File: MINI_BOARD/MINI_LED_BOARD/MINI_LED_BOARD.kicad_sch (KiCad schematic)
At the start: 38 parts, among them J1 Conn_ARM_SWD_TagConnect_TC2030, J2 430450428, U1 MSPM0C1103SDDFR, U2 TCAN334, U3 NCV891330PD50R2G, U4 TPS76333DBVR

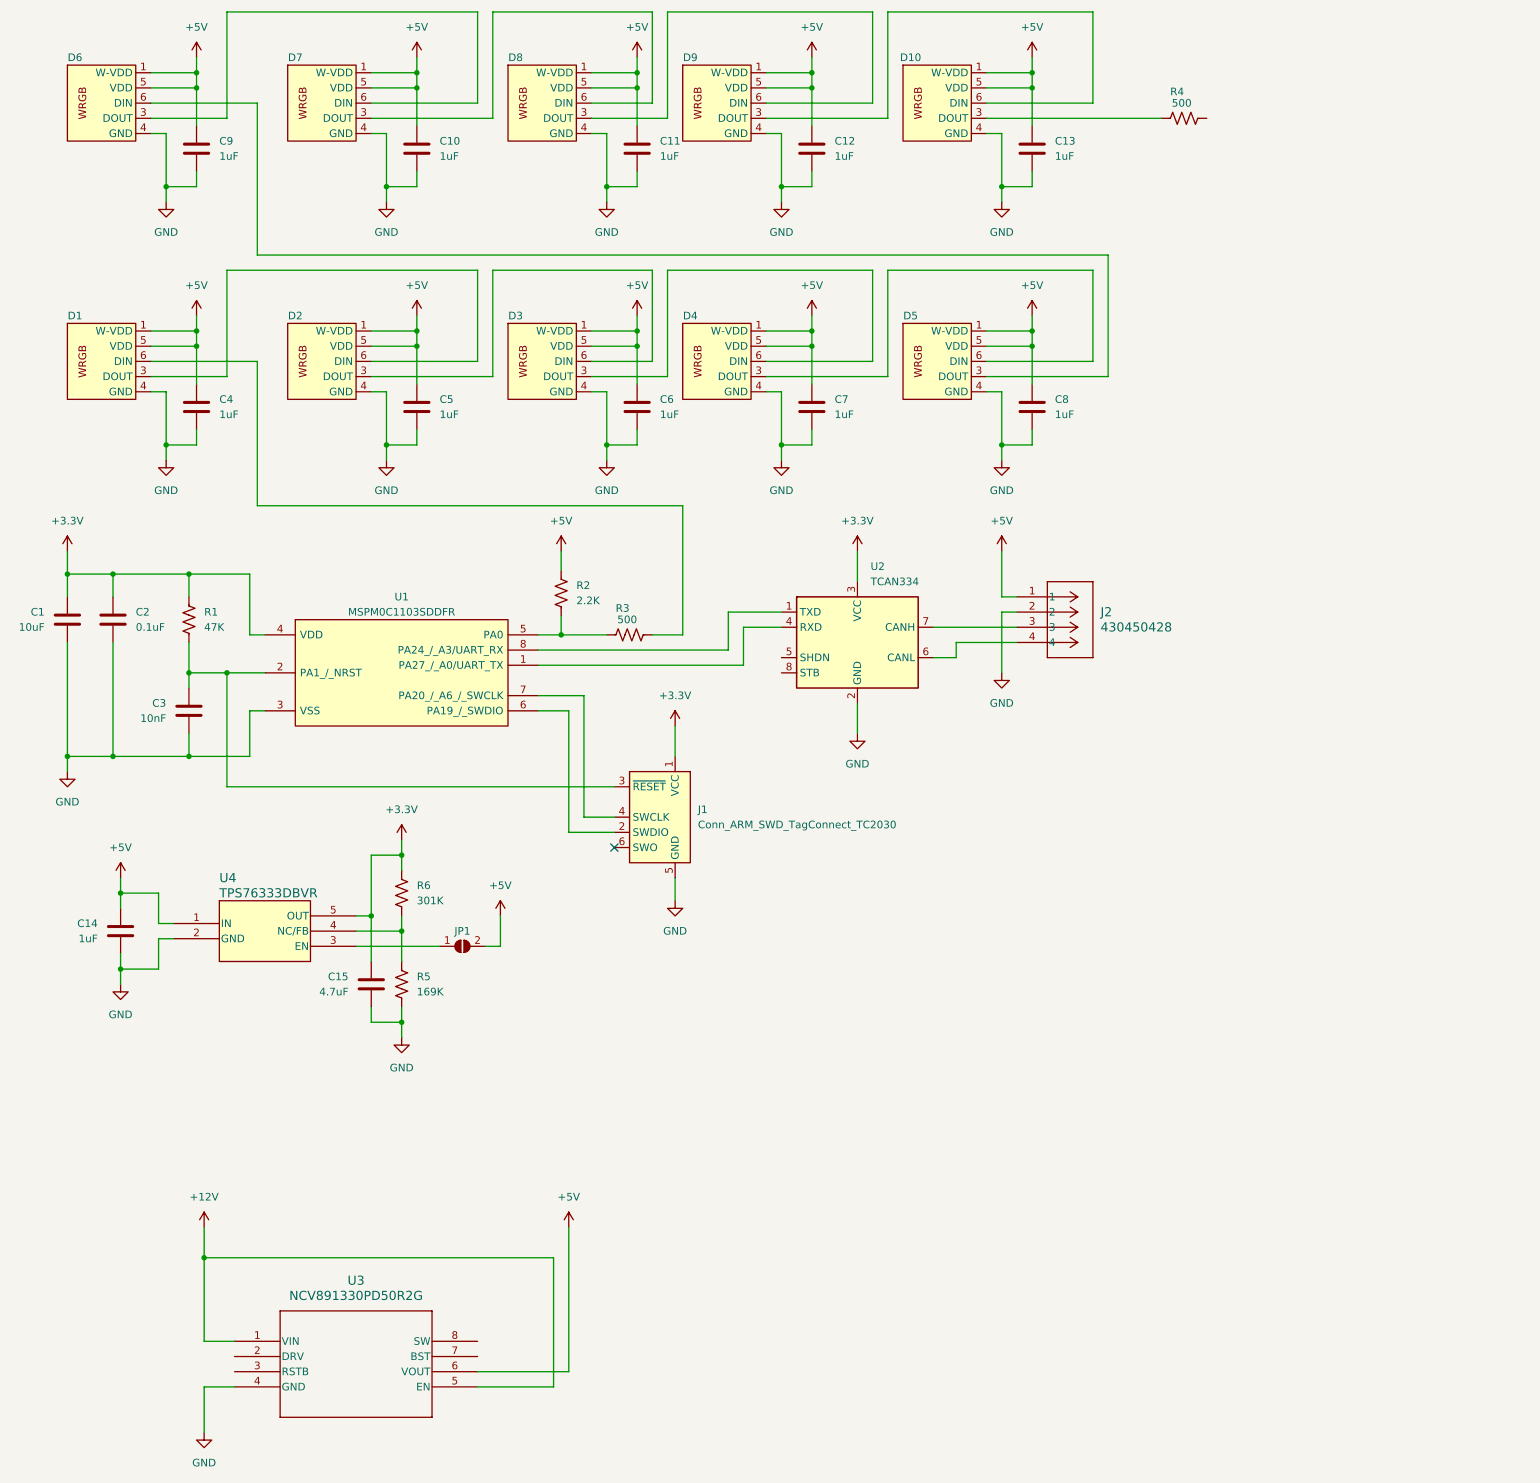
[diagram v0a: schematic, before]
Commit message: Add more footprints and adjust layout placements
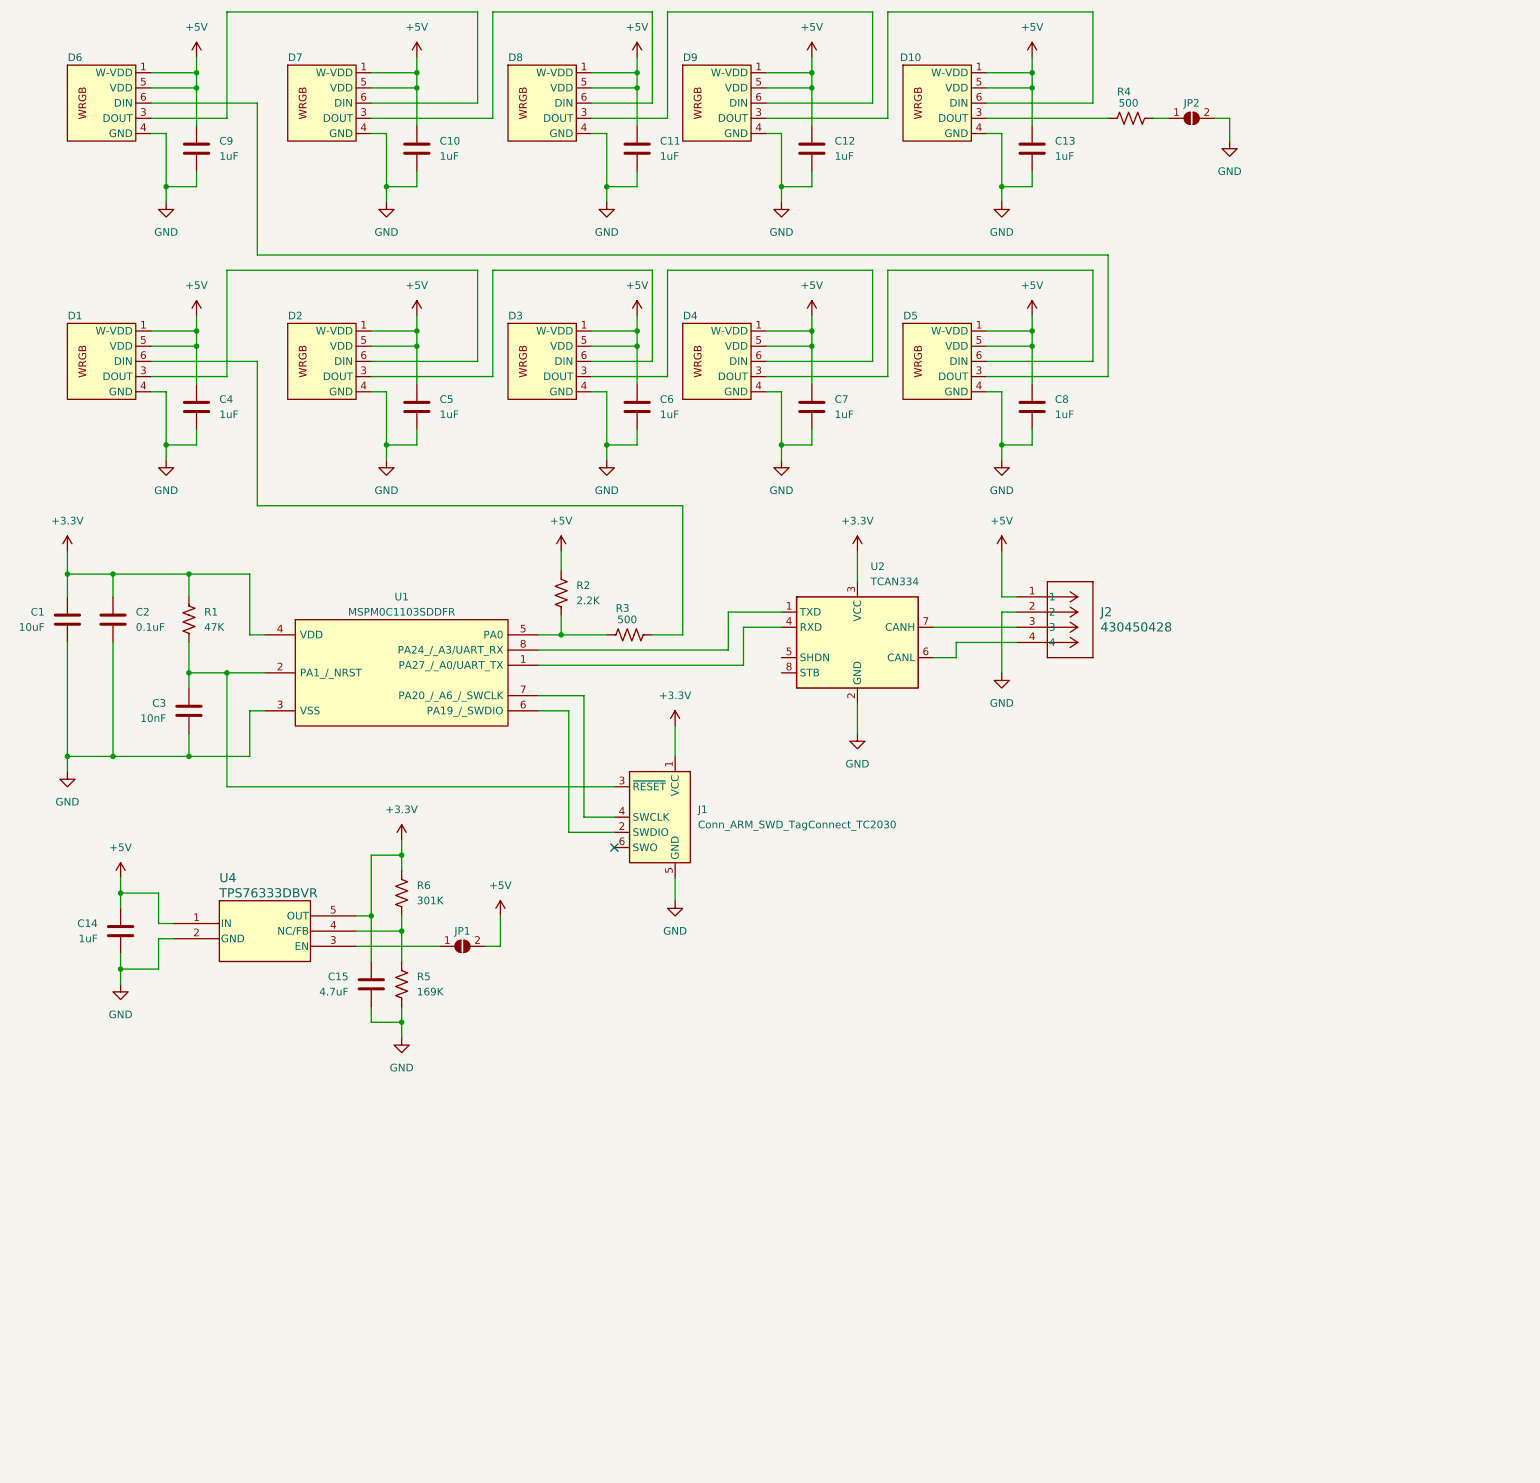
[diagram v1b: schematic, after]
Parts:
- removed U3: NCV891330PD50R2G, SOIC8_3P9X4P9_ONS, symbol NCV891330PD50R2G:NCV891330PD50R2G
- added JP2: SolderJumper_2_Open, Jumper:SolderJumper-2_P1.3mm_Open_RoundedPad1.0x1.5mm, symbol Jumper:SolderJumper_2_Open
- JP1: footprint (none) -> Jumper:SolderJumper-2_P1.3mm_Open_RoundedPad1.0x1.5mm
- U2: footprint (none) -> Package_TO_SOT_SMD:SOT-23-8_Handsoldering
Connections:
- net GND: now also JP2.2 (B)
- net at R4.2: now also JP2.1 (A)
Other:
- moved on the sheet: R4
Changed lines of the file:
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@@
   (junction (at 180.34 46.99) (diameter 0) (color 0 0 0 0)
   )
-  (junction (at 46.99 226.06) (diameter 0) (color 0 0 0 0)
-  )
   (junction (at 80.01 171.45) (diameter 0) (color 0 0 0 0)
   )
@@
     (stroke (width 0) (type default))
   )
-  (wire (pts (xy 107.95 245.11) (xy 107.95 220.98))
-    (stroke (width 0) (type default))
-  )
   (wire (pts (xy 143.51 49.53) (xy 143.51 46.99))
     (stroke (width 0) (type default))
@@
     (stroke (width 0) (type default))
   )
+  (wire (pts (xy 218.44 39.37) (xy 218.44 35.56))
+    (stroke (width 0) (type default))
+  )
   (wire (pts (xy 111.76 76.2) (xy 121.92 76.2))
     (stroke (width 0) (type default))
@@
     (stroke (width 0) (type default))
   )
-  (wire (pts (xy 52.07 247.65) (xy 46.99 247.65))
-    (stroke (width 0) (type default))
-  )
   (wire (pts (xy 95.25 35.56) (xy 95.25 17.78))
     (stroke (width 0) (type default))
@@
     (stroke (width 0) (type default))
   )
-  (wire (pts (xy 105.41 226.06) (xy 46.99 226.06))
-    (stroke (width 0) (type default))
-  )
   (wire (pts (xy 134.62 118.11) (xy 143.51 118.11))
     (stroke (width 0) (type default))
@@
     (stroke (width 0) (type default))
   )
-  (wire (pts (xy 105.41 247.65) (xy 105.41 226.06))
-    (stroke (width 0) (type default))
-  )
   (wire (pts (xy 185.42 71.12) (xy 185.42 68.58))
     (stroke (width 0) (type default))
@@
     (stroke (width 0) (type default))
   )
-  (wire (pts (xy 46.99 247.65) (xy 46.99 255.27))
-    (stroke (width 0) (type default))
-  )
   (wire (pts (xy 198.12 78.74) (xy 198.12 58.42))
     (stroke (width 0) (type default))
@@
     (stroke (width 0) (type default))
   )
-  (wire (pts (xy 52.07 240.03) (xy 46.99 240.03))
-    (stroke (width 0) (type default))
-  )
   (wire (pts (xy 44.45 111.76) (xy 44.45 115.57))
     (stroke (width 0) (type default))
@@
     (stroke (width 0) (type default))
   )
+  (wire (pts (xy 208.28 35.56) (xy 205.74 35.56))
+    (stroke (width 0) (type default))
+  )
   (wire (pts (xy 140.97 78.74) (xy 161.29 78.74))
     (stroke (width 0) (type default))
@@
     (stroke (width 0) (type default))
   )
-  (wire (pts (xy 177.8 35.56) (xy 207.01 35.56))
+  (wire (pts (xy 177.8 35.56) (xy 198.12 35.56))
     (stroke (width 0) (type default))
   )
@@
     (stroke (width 0) (type default))
   )
-  (wire (pts (xy 92.71 247.65) (xy 105.41 247.65))
-    (stroke (width 0) (type default))
-  )
   (wire (pts (xy 74.93 27.94) (xy 82.55 27.94))
     (stroke (width 0) (type default))
@@
     (stroke (width 0) (type default))
   )
-  (wire (pts (xy 46.99 226.06) (xy 46.99 220.98))
-    (stroke (width 0) (type default))
-  )
   (wire (pts (xy 185.42 27.94) (xy 185.42 25.4))
     (stroke (width 0) (type default))
@@
     (stroke (width 0) (type default))
   )
-  (wire (pts (xy 46.99 226.06) (xy 46.99 240.03))
-    (stroke (width 0) (type default))
-  )
   (wire (pts (xy 50.8 35.56) (xy 38.1 35.56))
     (stroke (width 0) (type default))
@@
     (stroke (width 0) (type default))
   )
+  (wire (pts (xy 218.44 35.56) (xy 215.9 35.56))
+    (stroke (width 0) (type default))
+  )
   (wire (pts (xy 95.25 78.74) (xy 95.25 60.96))
     (stroke (width 0) (type default))
@@
     (stroke (width 0) (type default))
   )
-  (wire (pts (xy 92.71 245.11) (xy 107.95 245.11))
-    (stroke (width 0) (type default))
-  )
   (wire (pts (xy 127 121.92) (xy 121.92 121.92))
     (stroke (width 0) (type default))
@@
     )
   )
-  (symbol (lib_id "Device:R_US") (at 210.82 35.56 90) (unit 1)
+  (symbol (lib_id "Device:R_US") (at 201.93 35.56 90) (unit 1)
     (in_bom yes) (on_board yes) (dnp no)
-    (property "Reference" "R4" (at 210.82 31.115 90)
+    (property "Reference" "R4" (at 201.93 31.115 90)
       (effects (font (size 1.27 1.27)) (justify left))
     )
-    (property "Value" "500" (at 212.09 33.02 90)
+    (property "Value" "500" (at 203.2 33.02 90)
       (effects (font (size 1.27 1.27)) (justify left))
     )
-    (property "Footprint" "Resistor_SMD:R_0603_1608Metric_Pad0.98x0.95mm_HandSolder" (at 211.074 34.544 90)
+    (property "Footprint" "Resistor_SMD:R_0603_1608Metric_Pad0.98x0.95mm_HandSolder" (at 202.184 34.544 90)
       (effects (font (size 1.27 1.27)) hide)
     )
-    (property "Datasheet" "~" (at 210.82 35.56 0)
+    (property "Datasheet" "~" (at 201.93 35.56 0)
       (effects (font (size 1.27 1.27)) hide)
     )
@@
     )
   )
-  (symbol (lib_id "power:GND") (at 46.99 255.27 0) (unit 1)
+  (symbol (lib_id "power:GND") (at 218.44 39.37 0) (unit 1)
     (in_bom yes) (on_board yes) (dnp no) (fields_autoplaced)
-    (property "Reference" "#PWR031" (at 46.99 261.62 0)
+    (property "Reference" "#PWR030" (at 218.44 45.72 0)
       (effects (font (size 1.27 1.27)) hide)
     )
-    (property "Value" "GND" (at 46.99 260.35 0)
+    (property "Value" "GND" (at 218.44 44.45 0)
       (effects (font (size 1.27 1.27)))
     )
-    (property "Footprint" "" (at 46.99 255.27 0)
+    (property "Footprint" "" (at 218.44 39.37 0)
       (effects (font (size 1.27 1.27)) hide)
     )
-    (property "Datasheet" "" (at 46.99 255.27 0)
+    (property "Datasheet" "" (at 218.44 39.37 0)
       (effects (font (size 1.27 1.27)) hide)
     )
@@
       (project "MINI_LED_BOARD"
         (path "/456c4893-77f2-49ff-a529-797b73777b2a"
-          (reference "#PWR031") (unit 1)
+          (reference "#PWR030") (unit 1)
+        )
+      )
+      (project "MINI_LED_BOARD"
+        (path "/c268a3d0-71f4-46b5-be8b-843057045928"
+          (reference "#PWR017") (unit 1)
         )
       )
       (project "CAN_LIGHT"
         (path "/d4f25219-6cef-4e47-aded-6c41d03d24e2"
-          (reference "#PWR099") (unit 1)
+          (reference "#PWR088") (unit 1)
         )
       )
@@
     )
   )
-  (symbol (lib_id "power:+5V") (at 107.95 220.98 0) (unit 1)
-    (in_bom yes) (on_board yes) (dnp no) (fields_autoplaced)
-    (property "Reference" "#PWR032" (at 107.95 224.79 0)
-      (effects (font (size 1.27 1.27)) hide)
-    )
-    (property "Value" "+5V" (at 107.95 215.9 0)
-      (effects (font (size 1.27 1.27)))
-    )
-    (property "Footprint" "" (at 107.95 220.98 0)
-      (effects (font (size 1.27 1.27)) hide)
-    )
-    (property "Datasheet" "" (at 107.95 220.98 0)
-      (effects (font (size 1.27 1.27)) hide)
-    )
-    (pin "1")
-    (instances
-      (project "MINI_LED_BOARD"
-        (path "/456c4893-77f2-49ff-a529-797b73777b2a"
-          (reference "#PWR032") (unit 1)
-        )
-      )
-      (project "CAN_LIGHT"
-        (path "/d4f25219-6cef-4e47-aded-6c41d03d24e2"
-          (reference "#PWR0100") (unit 1)
-        )
-      )
-    )
-  )
   (symbol (lib_id "power:GND") (at 33.02 180.34 0) (unit 1)
     (in_bom yes) (on_board yes) (dnp no) (fields_autoplaced)
@@
     )
   )
-  (symbol (lib_id "NCV891330PD50R2G:NCV891330PD50R2G") (at 52.07 240.03 0) (unit 1)
-    (in_bom yes) (on_board yes) (dnp no) (fields_autoplaced)
-    (property "Reference" "U3" (at 72.39 229.87 0)
-      (effects (font (size 1.524 1.524)))
-    )
-    (property "Value" "NCV891330PD50R2G" (at 72.39 232.41 0)
-      (effects (font (size 1.524 1.524)))
-    )
-    (property "Footprint" "SOIC8_3P9X4P9_ONS" (at 52.07 240.03 0)
-      (effects (font (size 1.27 1.27) italic) hide)
-    )
-    (property "Datasheet" "NCV891330PD50R2G" (at 52.07 240.03 0)
-      (effects (font (size 1.27 1.27) italic) hide)
-    )
-    (pin "1")
-    (pin "2")
-    (pin "3")
-    (pin "4")
-    (pin "5")
-    (pin "6")
-    (pin "7")
-    (pin "8")
-    (instances
-      (project "MINI_LED_BOARD"
-        (path "/456c4893-77f2-49ff-a529-797b73777b2a"
-          (reference "U3") (unit 1)
-        )
-      )
-      (project "CAN_LIGHT"
-        (path "/d4f25219-6cef-4e47-aded-6c41d03d24e2"
-          (reference "U4") (unit 1)
-        )
-      )
-    )
-  )
   (symbol (lib_id "power:GND") (at 125.73 166.37 0) (unit 1)
     (in_bom yes) (on_board yes) (dnp no) (fields_autoplaced)
@@
       (effects (font (size 1.27 1.27)) (justify left))
     )
-    (property "Footprint" "" (at 156.21 135.89 0)
+    (property "Footprint" "Package_TO_SOT_SMD:SOT-23-8_Handsoldering" (at 156.21 135.89 0)
       (effects (font (size 1.27 1.27) italic) hide)
     )
@@
     )
   )
-  (symbol (lib_id "power:+12V") (at 46.99 220.98 0) (unit 1)
-    (in_bom yes) (on_board yes) (dnp no) (fields_autoplaced)
-    (property "Reference" "#PWR030" (at 46.99 224.79 0)
-      (effects (font (size 1.27 1.27)) hide)
-    )
-    (property "Value" "+12V" (at 46.99 215.9 0)
+  (symbol (lib_id "Jumper:SolderJumper_2_Open") (at 212.09 35.56 0) (unit 1)
+    (in_bom yes) (on_board yes) (dnp no)
+    (property "Reference" "JP2" (at 212.09 33.02 0)
       (effects (font (size 1.27 1.27)))
     )
-    (property "Footprint" "" (at 46.99 220.98 0)
+    (property "Value" "SolderJumper_2_Open" (at 227.33 45.72 0)
+      (effects (font (size 1.27 1.27)) hide)
+    )
+    (property "Footprint" "Jumper:SolderJumper-2_P1.3mm_Open_RoundedPad1.0x1.5mm" (at 212.09 35.56 0)
       (effects (font (size 1.27 1.27)) hide)
     )
-    (property "Datasheet" "" (at 46.99 220.98 0)
+    (property "Datasheet" "~" (at 212.09 35.56 0)
       (effects (font (size 1.27 1.27)) hide)
     )
     (pin "1")
+    (pin "2")
     (instances
       (project "MINI_LED_BOARD"
         (path "/456c4893-77f2-49ff-a529-797b73777b2a"
-          (reference "#PWR030") (unit 1)
+          (reference "JP2") (unit 1)
         )
       )
       (project "CAN_LIGHT"
         (path "/d4f25219-6cef-4e47-aded-6c41d03d24e2"
-          (reference "#PWR098") (unit 1)
+          (reference "JP1") (unit 1)
         )
       )
@@
       (effects (font (size 1.27 1.27)) hide)
     )
-    (property "Footprint" "" (at 90.17 173.99 0)
+    (property "Footprint" "Jumper:SolderJumper-2_P1.3mm_Open_RoundedPad1.0x1.5mm" (at 90.17 173.99 0)
       (effects (font (size 1.27 1.27)) hide)
     )
